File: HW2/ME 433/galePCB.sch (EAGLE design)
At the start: 22 parts, among them J4 USB-MB-H

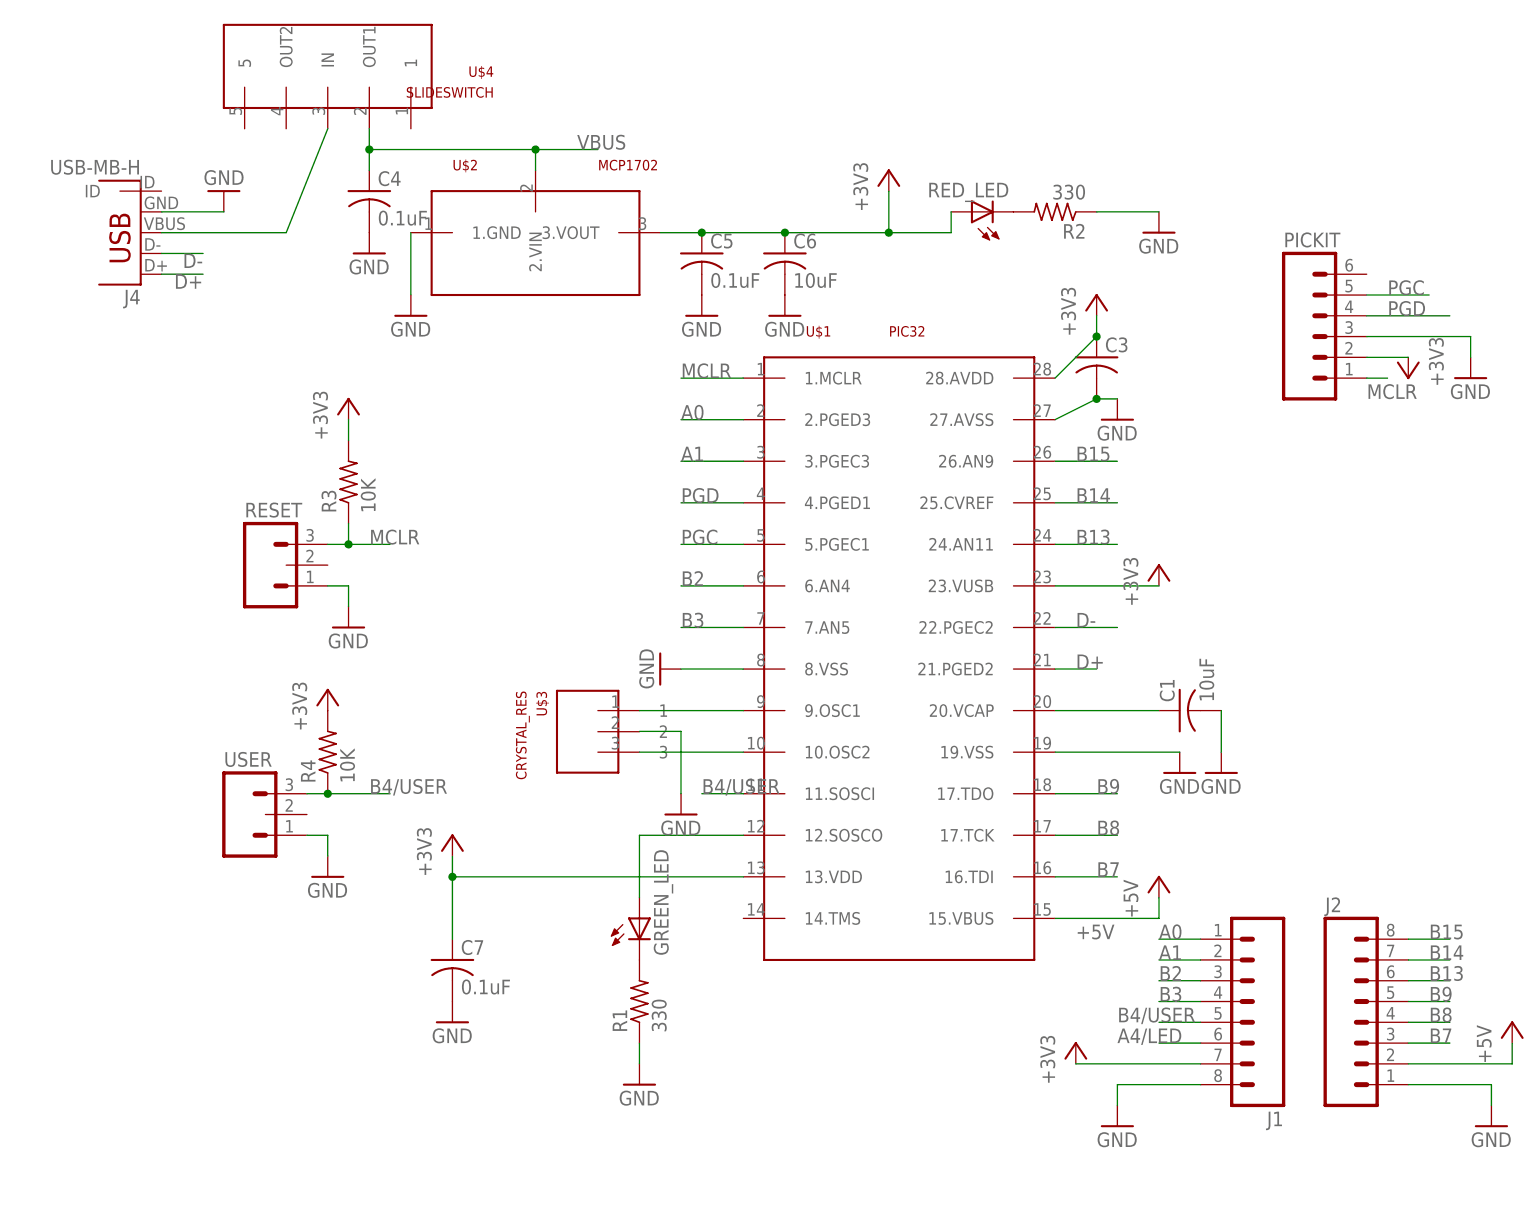
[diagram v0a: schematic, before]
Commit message: Continued editing of board
changed crystal oscillator to a M03, made all resistors smaller
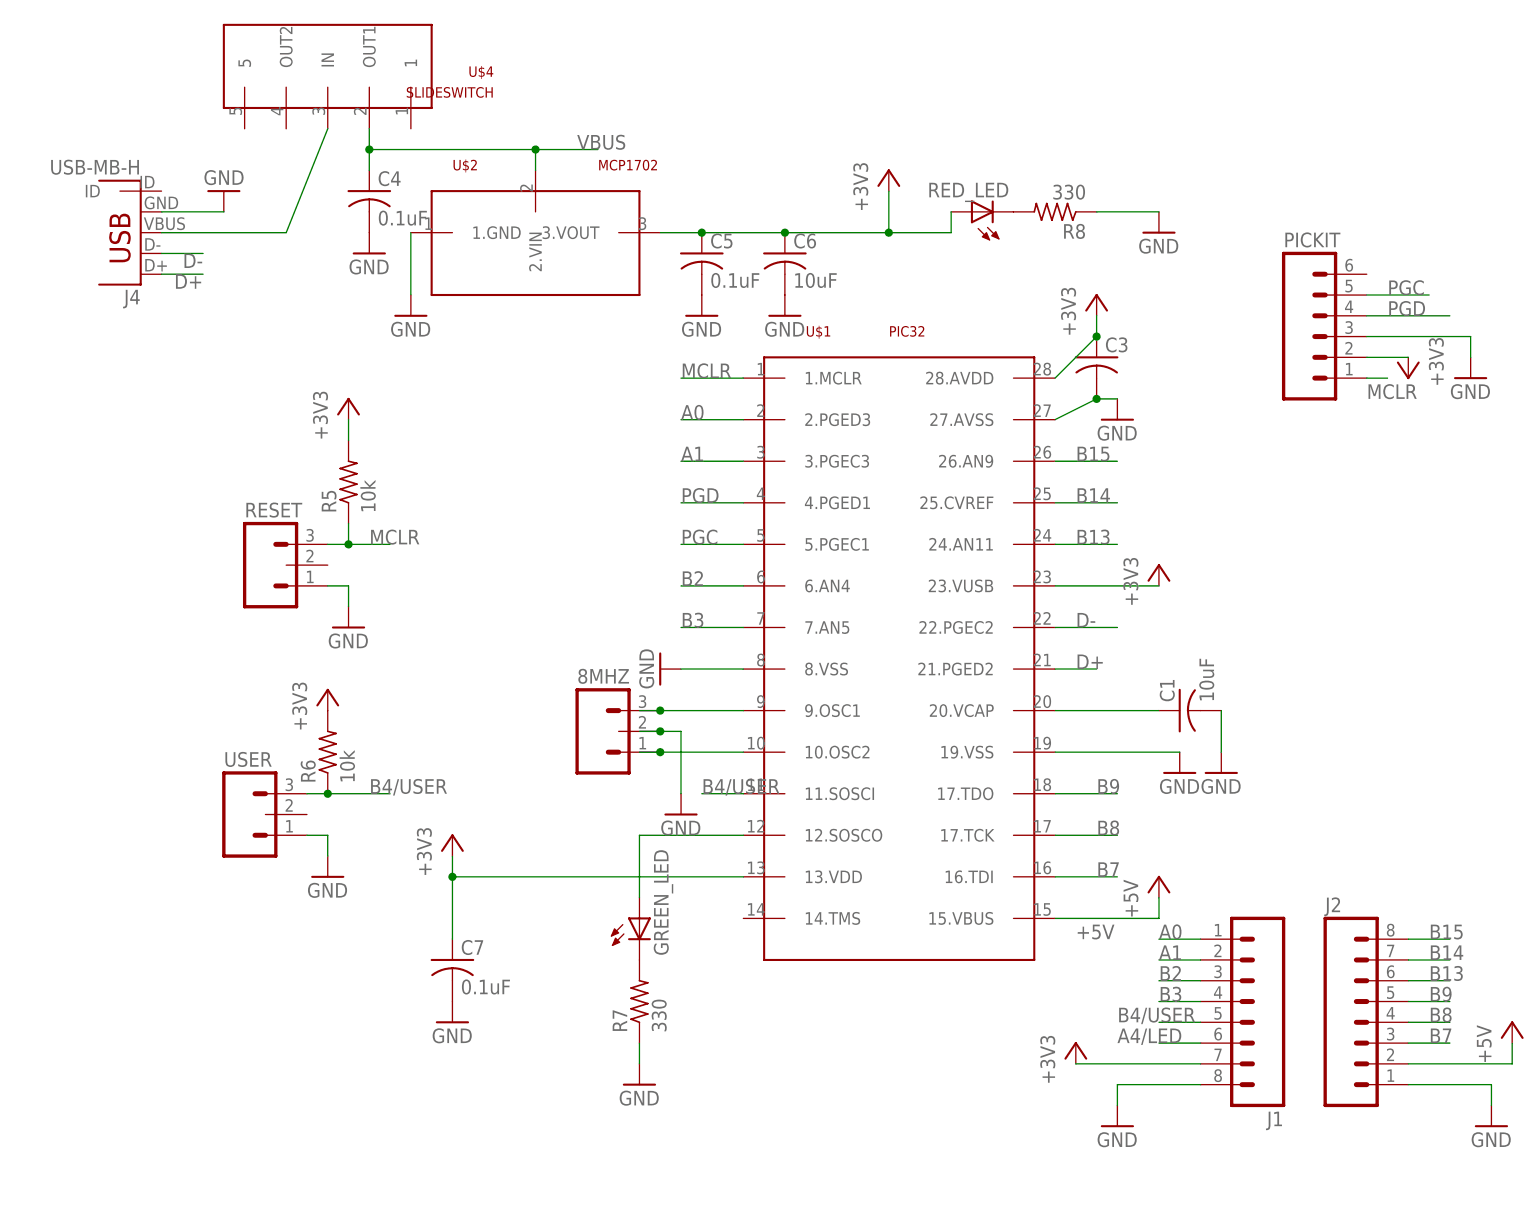
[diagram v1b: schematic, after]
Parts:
- removed R1, R2: 330, myPCB:R-US_0309/12
- removed R3, R4: 10K, myPCB:R-US_0309/12
- removed U$3: CRYSTAL_RES, myPCB:CRYSTAL_RES
- added 8MHZ: (no value), myPCB:M03PTH
- added R5, R6: 10k, myPCB:R-US_0207/10
- added R7, R8: 330, myPCB:R-US_0207/10
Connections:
- removed net N$8: GREEN_LED.C, R1.2
- new net N$6: GREEN_LED.C, R7.2
- net +3V3: now also R5.2, R6.2; no longer R3.2, R4.2
- net B4/USER: now also R6.1; no longer R4.1
- net GND: now also 8MHZ.2, R7.1, R8.1; no longer R1.1, R2.1
- net MCLR: now also R5.1; no longer R3.1
- net N$2: now also 8MHZ.3
- net N$3: now also 8MHZ.1
- net N$5: now also R8.2; no longer R2.2
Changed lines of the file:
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@@
 <part name="U$1" library="myPCB" deviceset="PIC32" device=""/>
 <part name="U$2" library="myPCB" deviceset="MCP1702" device=""/>
-<part name="U$3" library="myPCB" deviceset="CRYSTAL_RES" device=""/>
 <part name="RED_LED" library="myPCB" deviceset="LED" device="3MM"/>
 <part name="GREEN_LED" library="myPCB" deviceset="LED" device="3MM"/>
@@
 <part name="C1" library="myPCB" deviceset="C-US" device="025-024X044" value="10uF"/>
 <part name="C3" library="myPCB" deviceset="C-US" device="025-024X044"/>
-<part name="R1" library="myPCB" deviceset="R-US_" device="0309/12" value="330"/>
-<part name="R2" library="myPCB" deviceset="R-US_" device="0309/12" value="330"/>
-<part name="R3" library="myPCB" deviceset="R-US_" device="0309/12" value="10K"/>
-<part name="R4" library="myPCB" deviceset="R-US_" device="0309/12" value="10K"/>
 <part name="C4" library="myPCB" deviceset="C-US" device="025-024X044" value="0.1uF"/>
 <part name="C5" library="myPCB" deviceset="C-US" device="025-024X044" value="0.1uF"/>
@@
 <part name="GND18" library="myPCB" deviceset="GND" device=""/>
 <part name="P+2" library="myPCB" deviceset="+5V" device=""/>
+<part name="R5" library="myPCB" deviceset="R-US_" device="0207/10" value="10k"/>
+<part name="R6" library="myPCB" deviceset="R-US_" device="0207/10" value="10k"/>
+<part name="R7" library="myPCB" deviceset="R-US_" device="0207/10" value="330"/>
+<part name="R8" library="myPCB" deviceset="R-US_" device="0207/10" value="330"/>
+<part name="8MHZ" library="myPCB" deviceset="M03" device="PTH"/>
 </parts>
 <sheets>
@@
 <instance part="U$1" gate="G$1" x="66.04" y="50.8"/>
 <instance part="U$2" gate="G$1" x="25.4" y="96.52"/>
-<instance part="U$3" gate="G$1" x="33.02" y="33.02" rot="R270"/>
 <instance part="RED_LED" gate="G$1" x="78.74" y="99.06" rot="R90"/>
 <instance part="GREEN_LED" gate="G$1" x="38.1" y="12.7"/>
@@
 <instance part="C1" gate="G$1" x="104.14" y="38.1" rot="R90"/>
 <instance part="C3" gate="G$1" x="93.98" y="81.28"/>
-<instance part="R1" gate="G$1" x="38.1" y="2.54" rot="R90"/>
-<instance part="R2" gate="G$1" x="88.9" y="99.06" rot="R180"/>
-<instance part="R3" gate="G$1" x="2.54" y="66.04" rot="R90"/>
-<instance part="R4" gate="G$1" x="0" y="33.02" rot="R90"/>
 <instance part="C4" gate="G$1" x="5.08" y="101.6"/>
 <instance part="C5" gate="G$1" x="45.72" y="93.98"/>
@@
 <instance part="GND18" gate="1" x="10.16" y="86.36"/>
 <instance part="P+2" gate="1" x="101.6" y="17.78"/>
+<instance part="R5" gate="G$1" x="2.54" y="66.04" rot="R90"/>
+<instance part="R6" gate="G$1" x="0" y="33.02" rot="R90"/>
+<instance part="R7" gate="G$1" x="38.1" y="2.54" rot="R90"/>
+<instance part="R8" gate="G$1" x="88.9" y="99.06" rot="R180"/>
+<instance part="8MHZ" gate="J$1" x="33.02" y="35.56"/>
 </instances>
 <busses>
@@
 <segment>
 <pinref part="GND9" gate="1" pin="GND"/>
-<wire x1="38.1" y1="35.56" x2="43.18" y2="35.56" width="0.1524" layer="91"/>
+<wire x1="38.1" y1="35.56" x2="40.64" y2="35.56" width="0.1524" layer="91"/>
+<wire x1="40.64" y1="35.56" x2="43.18" y2="35.56" width="0.1524" layer="91"/>
 <wire x1="43.18" y1="35.56" x2="43.18" y2="27.94" width="0.1524" layer="91"/>
-</segment>
-<segment>
-<pinref part="R2" gate="G$1" pin="1"/>
+<pinref part="8MHZ" gate="J$1" pin="2"/>
+<junction x="40.64" y="35.56"/>
+</segment>
+<segment>
 <pinref part="GND11" gate="1" pin="GND"/>
 <wire x1="93.98" y1="99.06" x2="101.6" y2="99.06" width="0.1524" layer="91"/>
+<pinref part="R8" gate="G$1" pin="1"/>
 </segment>
 <segment>
@@
 </segment>
 <segment>
-<pinref part="R1" gate="G$1" pin="1"/>
 <pinref part="GND10" gate="1" pin="GND"/>
 <wire x1="38.1" y1="-2.54" x2="38.1" y2="-5.08" width="0.1524" layer="91"/>
+<pinref part="R7" gate="G$1" pin="1"/>
 </segment>
 <segment>
@@
 </segment>
 <segment>
-<pinref part="R3" gate="G$1" pin="2"/>
 <pinref part="+3V5" gate="G$1" pin="+3V3"/>
 <wire x1="2.54" y1="71.12" x2="2.54" y2="73.66" width="0.1524" layer="91"/>
+<pinref part="R5" gate="G$1" pin="2"/>
 </segment>
 <segment>
@@
 </segment>
 <segment>
-<pinref part="R4" gate="G$1" pin="2"/>
-<pinref part="+3V4" gate="G$1" pin="+3V3"/>
-</segment>
-<segment>
 <pinref part="U$1" gate="G$1" pin="23.VUSB"/>
 <pinref part="+3V1" gate="G$1" pin="+3V3"/>
@@
 <pinref part="+3V9" gate="G$1" pin="+3V3"/>
 <wire x1="91.44" y1="-5.08" x2="106.68" y2="-5.08" width="0.1524" layer="91"/>
+</segment>
+<segment>
+<pinref part="+3V4" gate="G$1" pin="+3V3"/>
+<pinref part="R6" gate="G$1" pin="2"/>
 </segment>
 </net>
@@
 <segment>
 <pinref part="RESET" gate="J$1" pin="3"/>
-<pinref part="R3" gate="G$1" pin="1"/>
 <wire x1="0" y1="58.42" x2="2.54" y2="58.42" width="0.1524" layer="91"/>
 <wire x1="2.54" y1="58.42" x2="2.54" y2="60.96" width="0.1524" layer="91"/>
@@
 <junction x="2.54" y="58.42"/>
 <label x="5.08" y="58.42" size="1.778" layer="95"/>
+<pinref part="R5" gate="G$1" pin="1"/>
 </segment>
 </net>
@@
 <segment>
 <pinref part="U$1" gate="G$1" pin="9.OSC1"/>
-<wire x1="38.1" y1="38.1" x2="50.8" y2="38.1" width="0.1524" layer="91"/>
+<wire x1="38.1" y1="38.1" x2="40.64" y2="38.1" width="0.1524" layer="91"/>
+<pinref part="8MHZ" gate="J$1" pin="3"/>
+<wire x1="40.64" y1="38.1" x2="50.8" y2="38.1" width="0.1524" layer="91"/>
+<junction x="40.64" y="38.1"/>
 </segment>
 </net>
@@
 <segment>
 <pinref part="U$1" gate="G$1" pin="10.OSC2"/>
-<wire x1="38.1" y1="33.02" x2="50.8" y2="33.02" width="0.1524" layer="91"/>
+<wire x1="38.1" y1="33.02" x2="40.64" y2="33.02" width="0.1524" layer="91"/>
+<pinref part="8MHZ" gate="J$1" pin="1"/>
+<wire x1="40.64" y1="33.02" x2="50.8" y2="33.02" width="0.1524" layer="91"/>
+<junction x="40.64" y="33.02"/>
 </segment>
 </net>
@@
 </segment>
 </net>
-<net name="N$5" class="0">
-<segment>
-<pinref part="RED_LED" gate="G$1" pin="C"/>
-<pinref part="R2" gate="G$1" pin="2"/>
-</segment>
-</net>
-<net name="N$8" class="0">
-<segment>
-<pinref part="GREEN_LED" gate="G$1" pin="C"/>
-<pinref part="R1" gate="G$1" pin="2"/>
-</segment>
-</net>
 <net name="B4/USER" class="0">
 <segment>
 <pinref part="USER" gate="J$1" pin="3"/>
+<label x="5.08" y="27.94" size="1.778" layer="95"/>
 <wire x1="-2.54" y1="27.94" x2="0" y2="27.94" width="0.1524" layer="91"/>
-<pinref part="R4" gate="G$1" pin="1"/>
-<label x="5.08" y="27.94" size="1.778" layer="95"/>
+<pinref part="R6" gate="G$1" pin="1"/>
 <wire x1="0" y1="27.94" x2="7.62" y2="27.94" width="0.1524" layer="91"/>
 <junction x="0" y="27.94"/>
@@
 </segment>
 </net>
+<net name="N$6" class="0">
+<segment>
+<pinref part="GREEN_LED" gate="G$1" pin="C"/>
+<pinref part="R7" gate="G$1" pin="2"/>
+</segment>
+</net>
+<net name="N$5" class="0">
+<segment>
+<pinref part="RED_LED" gate="G$1" pin="C"/>
+<pinref part="R8" gate="G$1" pin="2"/>
+</segment>
+</net>

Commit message: Finished Board positioning
Flipped one of the M08 header pins around to align with given
measurements, changed PICkit to a 5 pin header
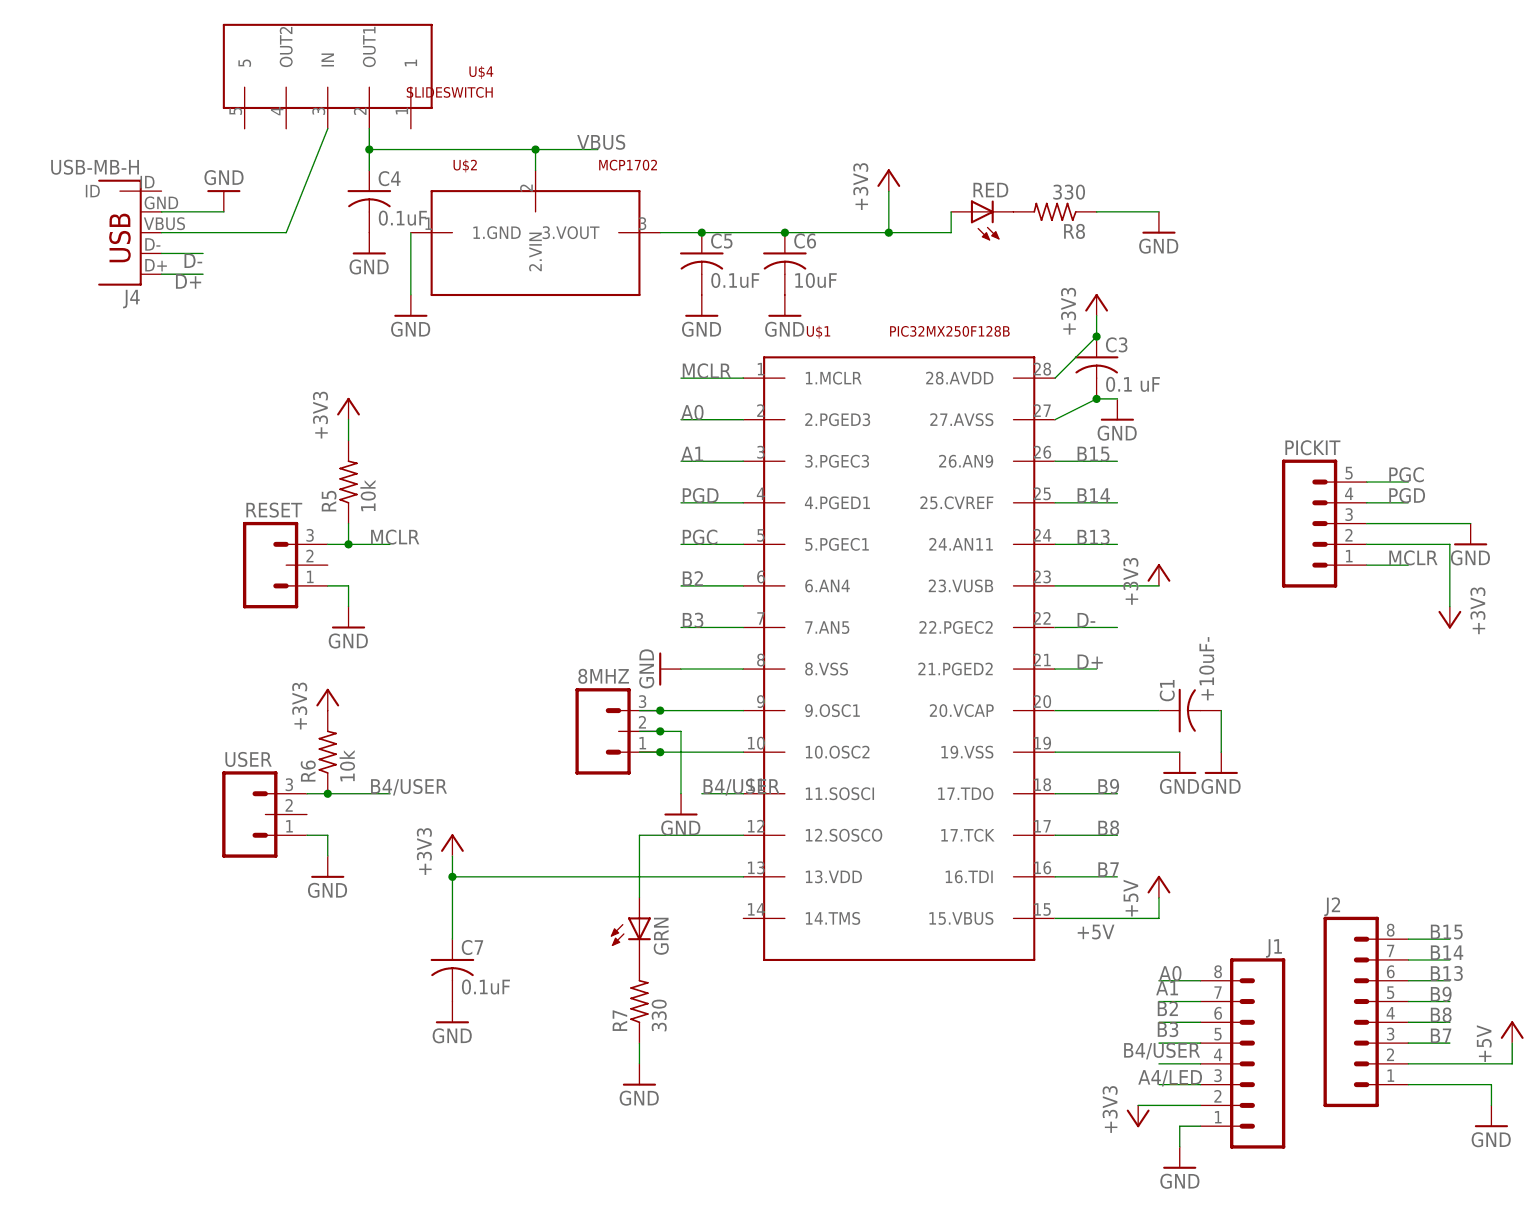
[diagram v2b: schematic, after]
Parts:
- C1: value 10uF -> +10uF-
- C3: value (none) -> 0.1 uF
- PICKIT: device myPCB:M06POLAR -> myPCB:M05PTH
- U$1: value PIC32 -> PIC32MX250F128B
- renumbered GREEN_LED to GRN, RED_LED to RED
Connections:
- net +3V3: now also J1.2; no longer J1.7
- net A0: now also J1.8; no longer J1.1
- net A1: now also J1.7; no longer J1.2
- net A4/LED: now also J1.3; no longer J1.6
- net B2: now also J1.6; no longer J1.3
- net B3: now also J1.5; no longer J1.4
- net B4/USER: now also J1.4; no longer J1.5
- net GND: now also J1.1; no longer J1.8
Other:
- moved on the sheet: J1

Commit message: Board Fully connected
May need to rotate switch, and need to write pin names on back of board
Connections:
- removed net N$4: GRN.A, U$1.12.SOSCO
- net A4/LED: now also GRN.A, U$1.12.SOSCO
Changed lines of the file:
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@@
-</segment>
-</net>
-<net name="N$4" class="0">
-<segment>
-<pinref part="U$1" gate="G$1" pin="12.SOSCO"/>
-<pinref part="GRN" gate="G$1" pin="A"/>
-<wire x1="50.8" y1="22.86" x2="38.1" y2="22.86" width="0.1524" layer="91"/>
-<wire x1="38.1" y1="22.86" x2="38.1" y2="15.24" width="0.1524" layer="91"/>
 </segment>
 </net>
@@
 <label x="99.06" y="-7.62" size="1.778" layer="95"/>
 </segment>
-</net>
+<segment>
+<pinref part="U$1" gate="G$1" pin="12.SOSCO"/>
+<pinref part="GRN" gate="G$1" pin="A"/>
+<wire x1="50.8" y1="22.86" x2="38.1" y2="22.86" width="0.1524" layer="91"/>
+<wire x1="38.1" y1="22.86" x2="38.1" y2="15.24" width="0.1524" layer="91"/>
+</segment>
+</net>
